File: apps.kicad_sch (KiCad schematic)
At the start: 53 parts, among them J1 Conn_01x08, J2 SWD, J3 UART, J4 Conn_01x04, Q1 AO3400A, SW1 SW_Push, SW2 SW_Push, U1 STM32F103C8Tx, U2 MCP2551, U3 AMS1117-5.0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

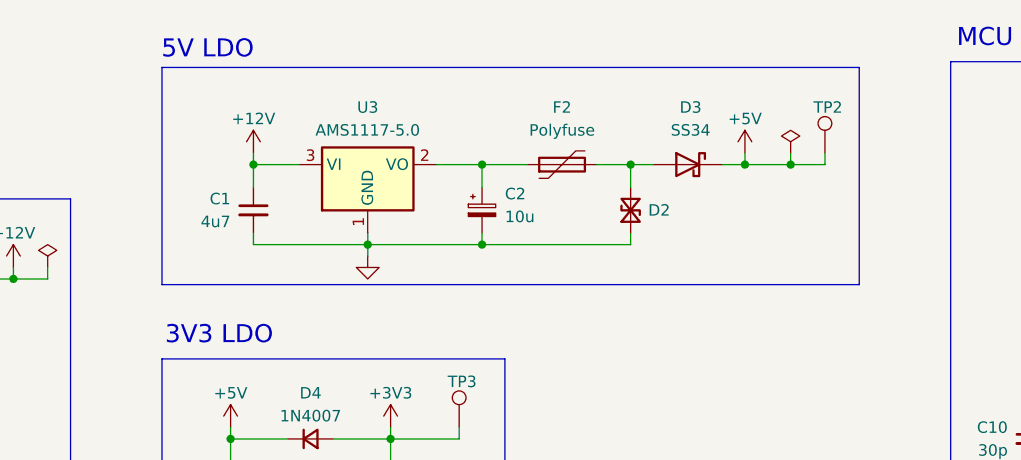
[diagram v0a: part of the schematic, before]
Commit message: schematic: Move C2 after D3
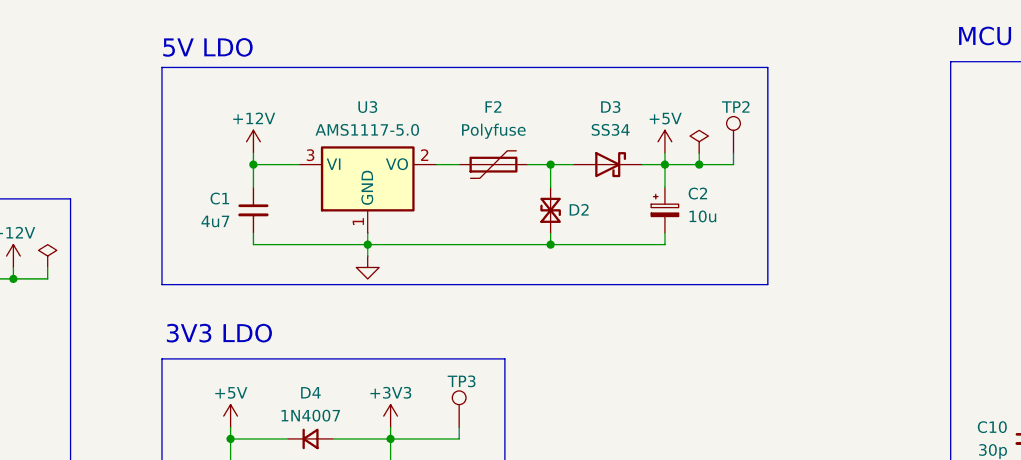
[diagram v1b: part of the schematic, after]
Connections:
- net +5V: now also C2.1
- net at F2.1, U3.2 (VO): no longer C2.1
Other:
- moved on the sheet: C2, D2, D3, F2, TP2

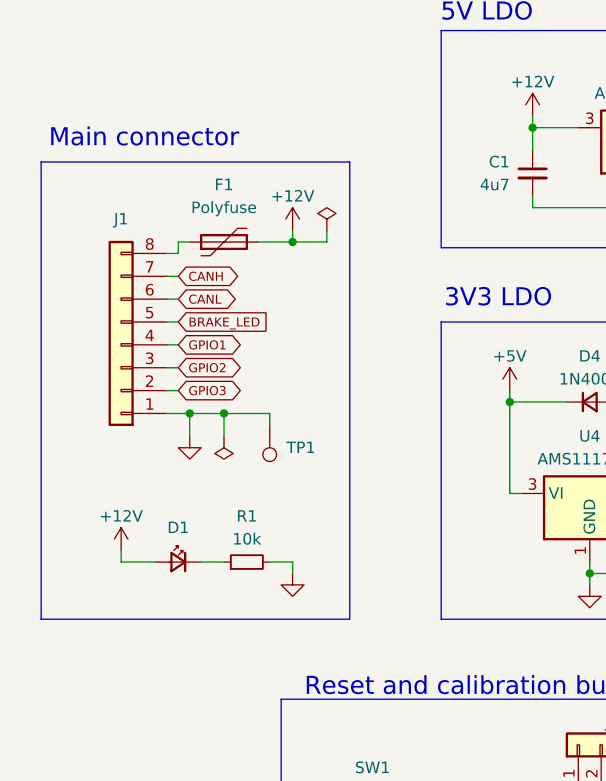
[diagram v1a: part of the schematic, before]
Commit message: schematic: Add another ESD TVS diode to 12V input
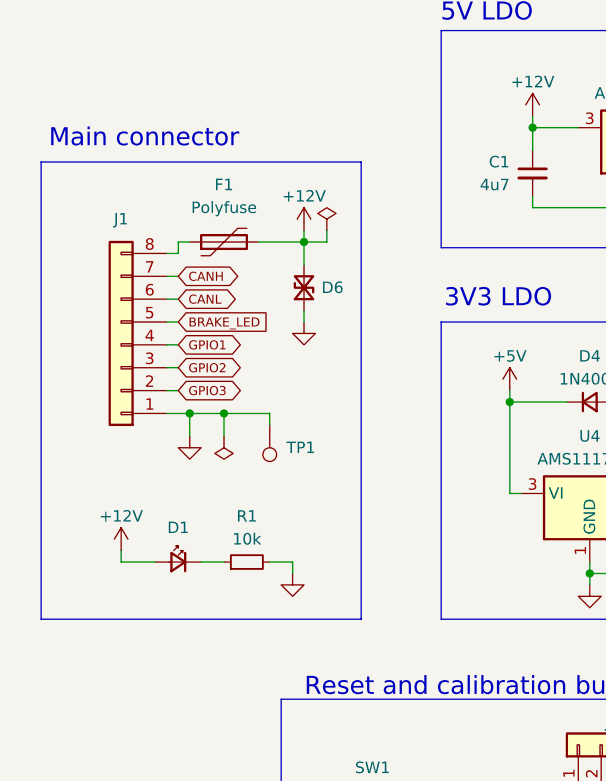
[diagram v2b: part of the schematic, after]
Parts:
- added D6: D_TVS_Small, symbol Device:D_TVS_Small
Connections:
- net +12V: now also D6.2 (A2)
- net GND: now also D6.1 (A1)
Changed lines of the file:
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@@
 	)
 	(junction
+		(at 53.34 49.53)
+		(diameter 0)
+		(color 0 0 0 0)
+	)
+	(junction
 		(at 107.95 111.76)
 		(diameter 0)
@@
 	)
 	(junction
-		(at 52.07 49.53)
-		(diameter 0)
-		(color 0 0 0 0)
-	)
-	(junction
 		(at 165.1 62.23)
 		(diameter 0)
@@
 	(wire
 		(pts
+			(xy 53.34 49.53) (xy 53.34 52.07)
+		)
+		(stroke
+			(width 0)
+			(type default)
+		)
+	)
+	(wire
+		(pts
 			(xy 93.98 66.04) (xy 93.98 67.31)
 		)
@@
 	(wire
 		(pts
-			(xy 55.88 49.53) (xy 52.07 49.53)
+			(xy 55.88 49.53) (xy 53.34 49.53)
 		)
 		(stroke
@@
 	(wire
 		(pts
+			(xy 53.34 57.15) (xy 53.34 58.42)
+		)
+		(stroke
+			(width 0)
+			(type default)
+		)
+	)
+	(wire
+		(pts
 			(xy 67.31 120.65) (xy 54.61 120.65)
 		)
@@
 	(wire
 		(pts
-			(xy 52.07 49.53) (xy 48.26 49.53)
+			(xy 48.26 49.53) (xy 53.34 49.53)
 		)
 		(stroke
@@
 	(wire
 		(pts
-			(xy 52.07 48.26) (xy 52.07 49.53)
+			(xy 53.34 48.26) (xy 53.34 49.53)
 		)
 		(stroke
@@
 	(rectangle
 		(start 24.13 40.64)
-		(end 58.42 91.44)
+		(end 59.69 91.44)
 		(stroke
 			(width 0)
@@
 	)
 	(symbol
+		(lib_id "Device:D_TVS_Small")
+		(at 53.34 54.61 90)
+		(unit 1)
+		(exclude_from_sim no)
+		(in_bom yes)
+		(on_board yes)
+		(dnp no)
+		(property "Reference" "D6"
+			(at 56.515 54.61 90)
+			(effects
+				(font
+					(size 1.27 1.27)
+				)
+			)
+		)
+		(property "Value" "D_TVS_Small"
+			(at 49.53 54.61 0)
+			(effects
+				(font
+					(size 1.27 1.27)
+				)
+				(hide yes)
+			)
+		)
+		(property "Footprint" ""
+			(at 53.34 54.61 0)
+			(effects
+				(font
+					(size 1.27 1.27)
+				)
+				(hide yes)
+			)
+		)
+		(property "Datasheet" "~"
+			(at 53.34 54.61 0)
+			(effects
+				(font
+					(size 1.27 1.27)
+				)
+				(hide yes)
+			)
+		)
+		(property "Description" "Bidirectional transient-voltage-suppression diode, small symbol"
+			(at 53.34 54.61 0)
+			(effects
+				(font
+					(size 1.27 1.27)
+				)
+				(hide yes)
+			)
+		)
+		(pin "2"
+		)
+		(pin "1"
+		)
+		(instances
+			(project "apps"
+				(path "/37c0128e-0bf6-47e1-84ea-e330ce83485d"
+					(reference "D6")
+					(unit 1)
+				)
+			)
+		)
+	)
+	(symbol
 		(lib_id "Device:C_Small")
 		(at 222.25 132.08 0)
@@
 	(symbol
 		(lib_id "power:+12V")
-		(at 52.07 48.26 0)
+		(at 53.34 48.26 0)
 		(unit 1)
 		(exclude_from_sim no)
@@
 		(dnp no)
 		(property "Reference" "#PWR01"
-			(at 52.07 52.07 0)
+			(at 53.34 52.07 0)
 			(effects
 				(font
@@
 		)
 		(property "Value" "+12V"
-			(at 52.07 44.45 0)
+			(at 53.34 44.45 0)
 			(effects
 				(font
@@
 		)
 		(property "Footprint" ""
-			(at 52.07 48.26 0)
+			(at 53.34 48.26 0)
 			(effects
 				(font
@@
 		)
 		(property "Datasheet" ""
-			(at 52.07 48.26 0)
+			(at 53.34 48.26 0)
 			(effects
 				(font
@@
 		)
 		(property "Description" "Power symbol creates a global label with name \"+12V\""
-			(at 52.07 48.26 0)
+			(at 53.34 48.26 0)
 			(effects
 				(font
@@
 					(unit 1)
 				)
+			)
+		)
+	)
+	(symbol
+		(lib_id "power:GND")
+		(at 53.34 58.42 0)
+		(unit 1)
+		(exclude_from_sim no)
+		(in_bom yes)
+		(on_board yes)
+		(dnp no)
+		(fields_autoplaced yes)
+		(property "Reference" "#PWR045"
+			(at 53.34 64.77 0)
+			(effects
+				(font
+					(size 1.27 1.27)
+				)
+				(hide yes)
+			)
+		)
+		(property "Value" "GND"
+			(at 53.34 63.5 0)
+			(effects
+				(font
+					(size 1.27 1.27)
+				)
+				(hide yes)
+			)
+		)
+		(property "Footprint" ""
+			(at 53.34 58.42 0)
+			(effects
+				(font
+					(size 1.27 1.27)
+				)
+				(hide yes)
+			)
+		)
+		(property "Datasheet" ""
+			(at 53.34 58.42 0)
+			(effects
+				(font
+					(size 1.27 1.27)
+				)
+				(hide yes)
+			)
+		)
+		(property "Description" "Power symbol creates a global label with name \"GND\" , ground"
+			(at 53.34 58.42 0)
+			(effects
+				(font
+					(size 1.27 1.27)
+				)
+				(hide yes)
+			)
+		)
+		(pin "1"
+		)
+		(instances
+			(project "apps"
+				(path "/37c0128e-0bf6-47e1-84ea-e330ce83485d"
+					(reference "#PWR045")
+					(unit 1)
+				)
